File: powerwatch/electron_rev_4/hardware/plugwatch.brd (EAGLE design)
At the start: 52.8 x 90.9 mm, 125 parts, among them J1 DM3AT-SF-PEJM5, Q1 SI223DDS, U1 BGA725L6-ALT, U10 SIP32510, U11 SN74AHC1G04DCKR, U12 SIP32510, U13 AB1815-T3, U16 MAX6746, U2 SAFFB1G56KB0F0A, U3 IRM-03-5V, U4 MAX-M8, U5 MAX9910, U6 LIS2DW12, U8 MAX9910, U9 SIP32510, X1 ABS07-32.768KHZ-7-T

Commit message: doing routing
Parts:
- removed Q1: SI223DDS, fets:SOT23-3
- removed R20: 10k, passives:0402_RES
- removed SJ1: (no value), jumper:SJW
- removed U11: SN74AHC1G04DCKR, chips:SC70
- added C4: 1uF, passives:0402_CAP
- C1, C24, C29, C3: device passives:0603_CAP -> passives:0402_CAP
- moved R1 90.3 mm to (30.0, 61.2), turned to 90 degrees
- moved C19 62.5 mm to (21.6, 72.6), flipped to the top, turned to 0 degrees
- moved C13 58.4 mm to (21.6, 69.2), flipped to the top, turned to 0 degrees
- moved TP13 57.7 mm to (-15.2, 17.0)
- moved R10 51.4 mm to (19.6, 67.6), flipped to the top, turned to 180 degrees
- moved R9 50.7 mm to (23.0, 67.6), flipped to the top, turned to 0 degrees
- moved ASSY1 50.4 mm to (51.7, 84.6), turned to 180 degrees
- moved C100 47.9 mm to (41.8, 9.40), turned to 270 degrees
- moved RI4 44.4 mm to (39.2, 9.40), turned to 270 degrees
- moved R18 42.0 mm to (39.9, 53.5), flipped to the top
- moved RI3 41.0 mm to (36.7, 9.40), turned to 270 degrees
- moved R6 40.9 mm to (3.94, 74.9), turned to 180 degrees
- moved C7 38.6 mm to (50.4, 15.7)
- moved R19 37.7 mm to (51.9, 61.6), flipped to the top, turned to 270 degrees
- moved RF1 37.5 mm to (34.2, 9.40), turned to 270 degrees
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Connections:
- removed net !RTC_INT2: R20.2, U13.4
- removed net N$35: J4.2, Q1.3, SJ1.2
- removed net N$9: Q1.1, U11.4
- net !EXTERNAL_RST: no longer U11.2
- net GND: now also C4.2; no longer U11.3
- net N$23: now also J4.2; no longer Q1.2, SJ1.1, U11.5
- net VCC: now also C4.1; no longer R20.1
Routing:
- net WDI: track 0.00 -> 63.3 mm
- net WIFI_PWR_EN: track 12.9 -> 72.9 mm
- net WIFI_TXD: track 10.8 -> 56.0 mm
- net !RTC_INT1: track 0.00 -> 44.2 mm, vias 0 -> 1
- net WIFI_RXD: track 1.80 -> 45.2 mm
- net SD_MOSI: track 5.78 -> 44.1 mm, vias 2 -> 1
- net SD_MISO: track 6.63 -> 44.0 mm
- net N$23: track 0.00 -> 34.8 mm
- net VCC: track 10.8 -> 41.1 mm, vias 2 -> 5
- net SD_SCLK: track 0.69 -> 25.5 mm, vias 2 -> 0
- net !EXTERNAL_RST: track 0.00 -> 21.7 mm, vias 0 -> 1
- net !GPS_RESET: track 7.07 -> 28.5 mm
- net MIC_WS: track 0.00 -> 20.6 mm
- net GPS_PWR_EN: track 6.30 -> 23.6 mm
- net GPS_VCC: track 19.8 -> 3.14 mm
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- added copper zone on layer 1, net GPS_VCC

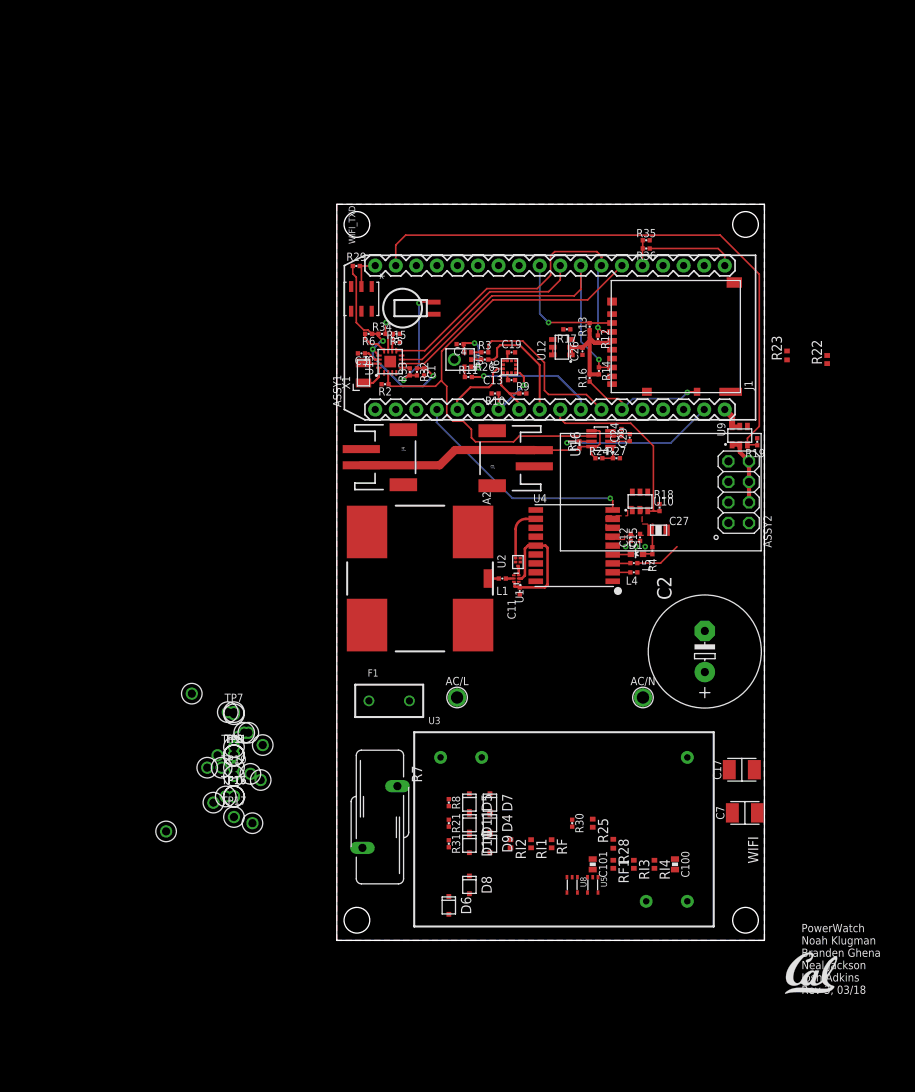
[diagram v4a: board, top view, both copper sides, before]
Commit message: almost finished routing - still need to do debug signals
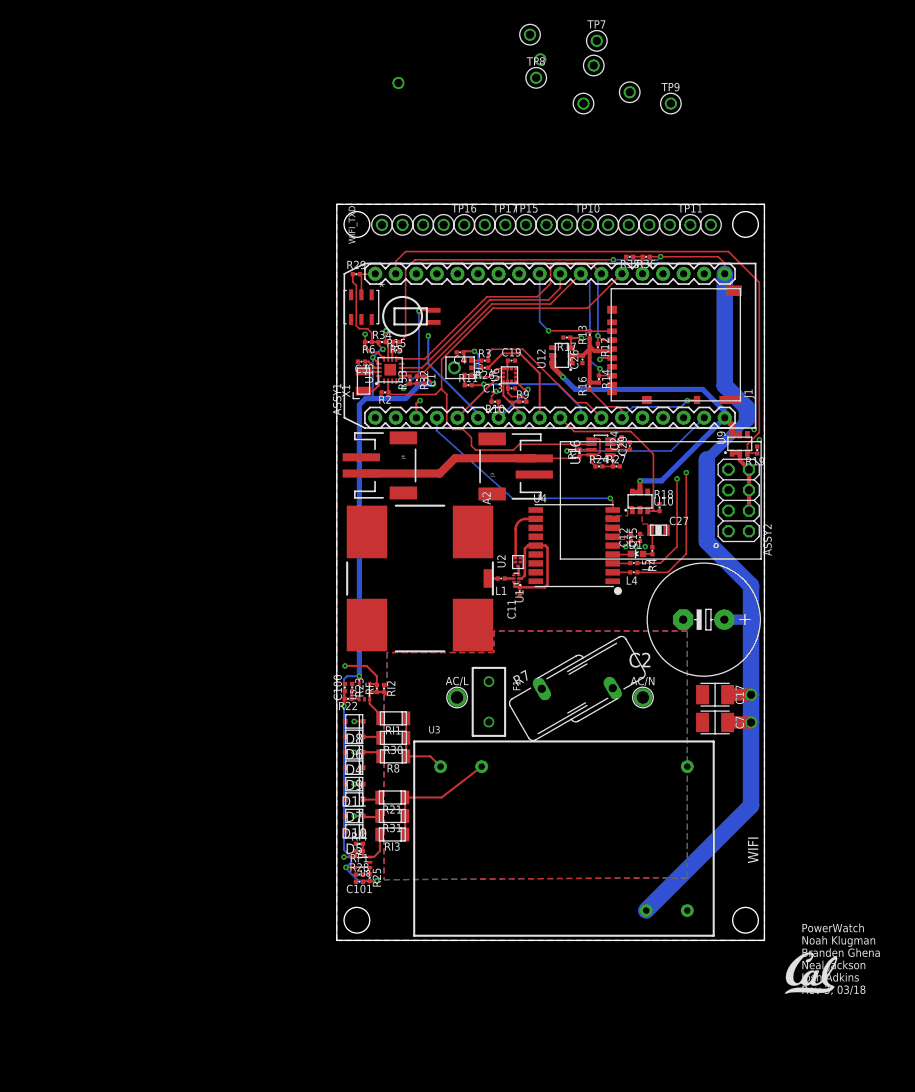
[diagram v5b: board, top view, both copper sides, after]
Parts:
- C100, C101: device passives:0603_CAP -> passives:0402_CAP
- J1: value DM3AT-SF-PEJM5 -> CON_MICRO_SDDM3AT-SF-PEJM5
- R21, R30, R31, R8: device passives:0402_RES -> passives:1206_RES_HIGH_CLEARANCE
- R22, R25, RF, RF1, RI2, RI4: device rcl:R0402 -> passives:0402_RES
- R23, R28: device rcl:R0402_SM -> passives:0402_RES
- RI1, RI3: device rcl:R0402 -> passives:1206_RES_HIGH_CLEARANCE
- U5, U8: value MAX9910 -> OPA369
- moved TP9 96.9 mm to (41.3, 103.4)
- moved TP7 94.5 mm to (32.1, 111.1)
- moved TP18 92.3 mm to (36.2, 104.8)
- moved TP1 91.6 mm to (23.9, 111.9)
- moved TP5 91.6 mm to (25.1, 108.8)
- moved TP8 91.6 mm to (24.6, 106.6)
- moved TP26 91.4 mm to (31.8, 108.1)
- moved TP24 88.1 mm to (41.1, 88.4)
- moved TP4 88.1 mm to (30.5, 103.4)
- moved TP2 87.4 mm to (46.2, 88.4)
- moved TP11 86.5 mm to (43.7, 88.4)
- moved TP3 86.0 mm to (7.62, 105.9)
- moved TP23 85.4 mm to (38.6, 88.4)
- moved TP6 82.9 mm to (36.1, 88.4)
- moved TP10 80.9 mm to (31.0, 88.4)
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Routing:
- net VCC: track 41.1 -> 195.4 mm, vias 5 -> 12
- net 5V: track 10.9 -> 151.1 mm, vias 0 -> 4
- net AC/N-PERTURB: track 0.00 -> 87.4 mm, vias 0 -> 1
- net AC/N-SENSE: track 0.00 -> 83.3 mm, vias 0 -> 1
- net AC/N-MEASURE: track 0.00 -> 82.5 mm, vias 0 -> 1
- net AC/L-PERTURB: track 0.00 -> 81.7 mm, vias 0 -> 1
- net AC/L-MEASURE: track 0.00 -> 75.0 mm, vias 0 -> 1
- net AC/L-SENSE: track 0.00 -> 70.7 mm, vias 0 -> 1
- net GPS_TXD: track 0.00 -> 42.8 mm, vias 0 -> 1
- net AC/N-FUSED: track 0.00 -> 39.7 mm
- net GPS_RXD: track 5.74 -> 41.9 mm, vias 0 -> 1
- net SD_ENABLE: track 0.00 -> 28.8 mm, vias 0 -> 2
- net AC/L-FUSED: track 0.00 -> 26.0 mm
- net !RTC_CS: track 3.55 -> 26.4 mm, vias 0 -> 2
- net SD_SCLK: track 25.5 -> 39.7 mm, vias 0 -> 1
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- added copper zone on layer 1, net N$7
- added copper zone on layer 15, net N$7
- added copper zone on layer 16, net N$7
- added copper zone on layer 2, net N$7

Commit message: layed out debug header, most of the way done routing
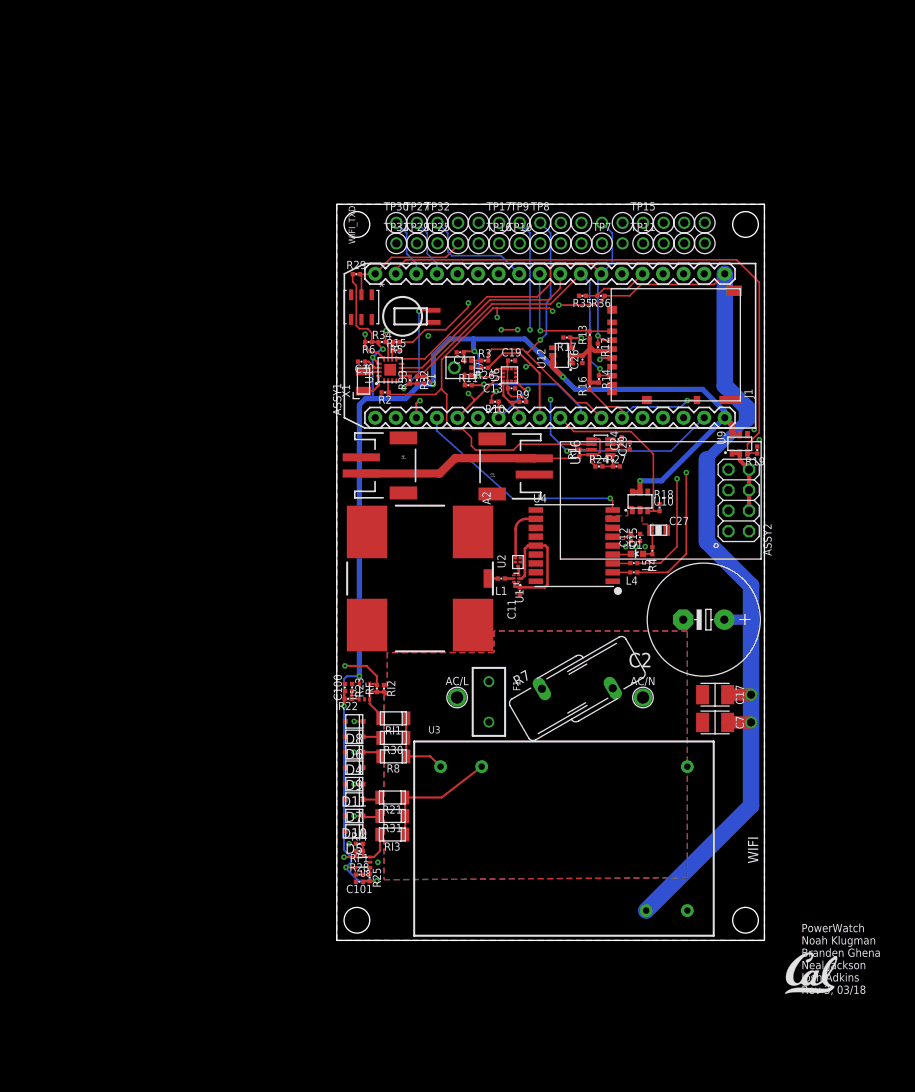
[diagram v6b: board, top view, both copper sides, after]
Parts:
- added TP25, TP27, TP29, TP30, TP31, TP32: TEST_POINT_0.040IN, headers:TESTPOINT_0.040IN
- moved TP3 30.5 mm to (32.8, 88.6)
- moved TP1 30.1 mm to (42.9, 88.6)
- moved TP26 25.9 mm to (45.5, 86.1)
- moved TP7 25.0 mm to (32.8, 86.1)
- moved TP5 24.9 mm to (35.3, 86.1)
- moved TP9 23.8 mm to (22.6, 88.6)
- moved TP18 18.6 mm to (45.5, 88.6)
- moved TP8 17.9 mm to (25.1, 88.6)
- moved TP4 15.5 mm to (35.3, 88.6)
- moved TP15 14.5 mm to (37.8, 88.6)
- moved TP24 10.9 mm to (30.2, 88.6)
- moved TP14 9.67 mm to (17.5, 86.1)
- moved TP19 9.67 mm to (27.7, 86.1)
- moved TP28 9.67 mm to (15.0, 86.1)
- moved TP10 8.69 mm to (22.6, 86.1)
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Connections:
- net AC/L-MEASURE: now also TP29.TESTPOINT
- net AC/L-PERTURB: now also TP25.TESTPOINT
- net AC/L-SENSE: now also TP31.TESTPOINT
- net AC/N-MEASURE: now also TP27.TESTPOINT
- net AC/N-PERTURB: now also TP32.TESTPOINT
- net AC/N-SENSE: now also TP30.TESTPOINT
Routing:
- net !EXTERNAL_RST: track 21.7 -> 53.4 mm, vias 1 -> 2
- net ACCEL_INT: track 7.76 -> 38.9 mm, vias 0 -> 1
- net WIFI_TXD: track 56.0 -> 85.8 mm
- net WIFI_RXD: track 45.2 -> 70.9 mm
- net VCC: track 195.4 -> 220.9 mm
- net MIC_BCLK: track 16.0 -> 38.4 mm, vias 1 -> 3
- net MIC_DATA: track 13.6 -> 33.0 mm, vias 0 -> 2
- net MIC_WS: track 18.6 -> 36.6 mm, vias 0 -> 1
- net AC/N-PERTURB: track 87.4 -> 101.4 mm
- net SERIAL_NUM: track 4.55 -> 16.5 mm
- net WDI: track 63.3 -> 75.0 mm, vias 0 -> 2
- net WIFI_PWR_EN: track 71.4 -> 82.2 mm
- net SD_MISO: track 42.4 -> 51.8 mm
- net AC/L-MEASURE: track 75.0 -> 84.4 mm
- net SD_SCLK: track 39.7 -> 48.9 mm
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
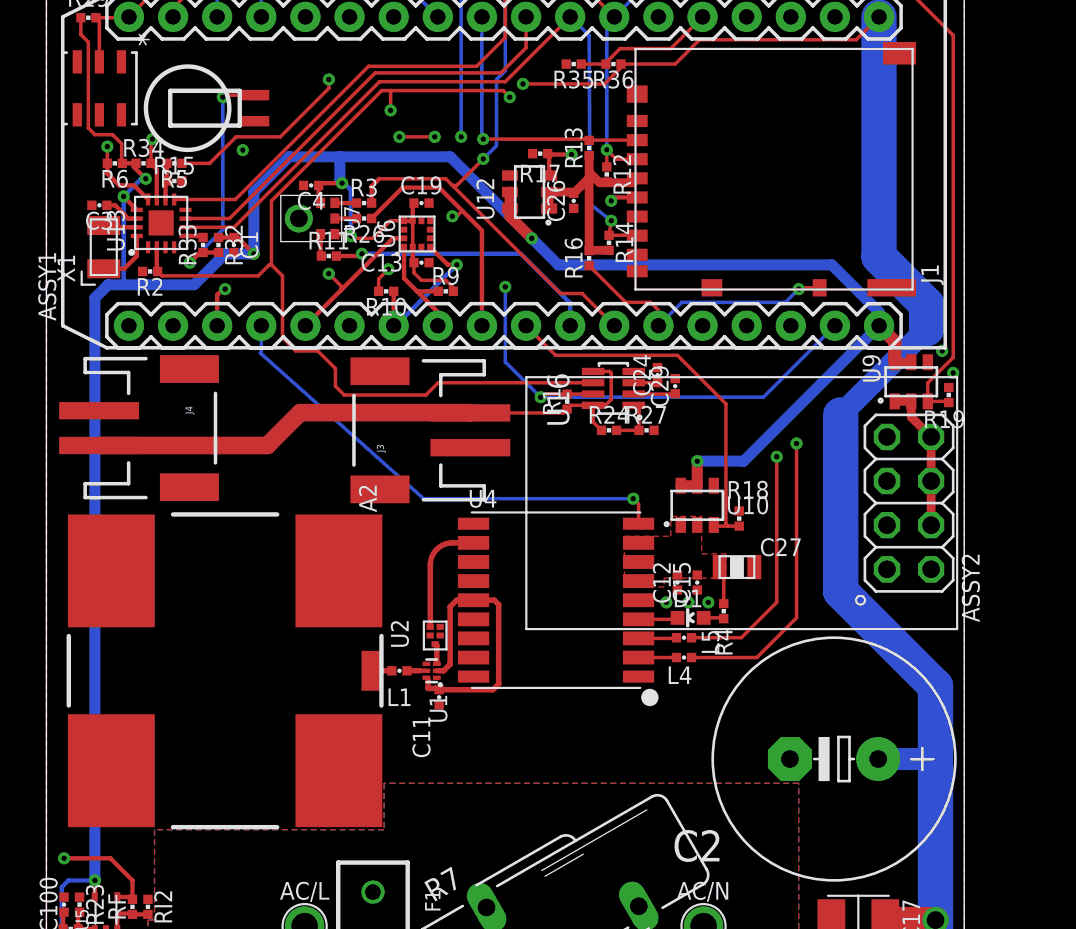
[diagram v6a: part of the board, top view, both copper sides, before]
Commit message: only 4 more airwires
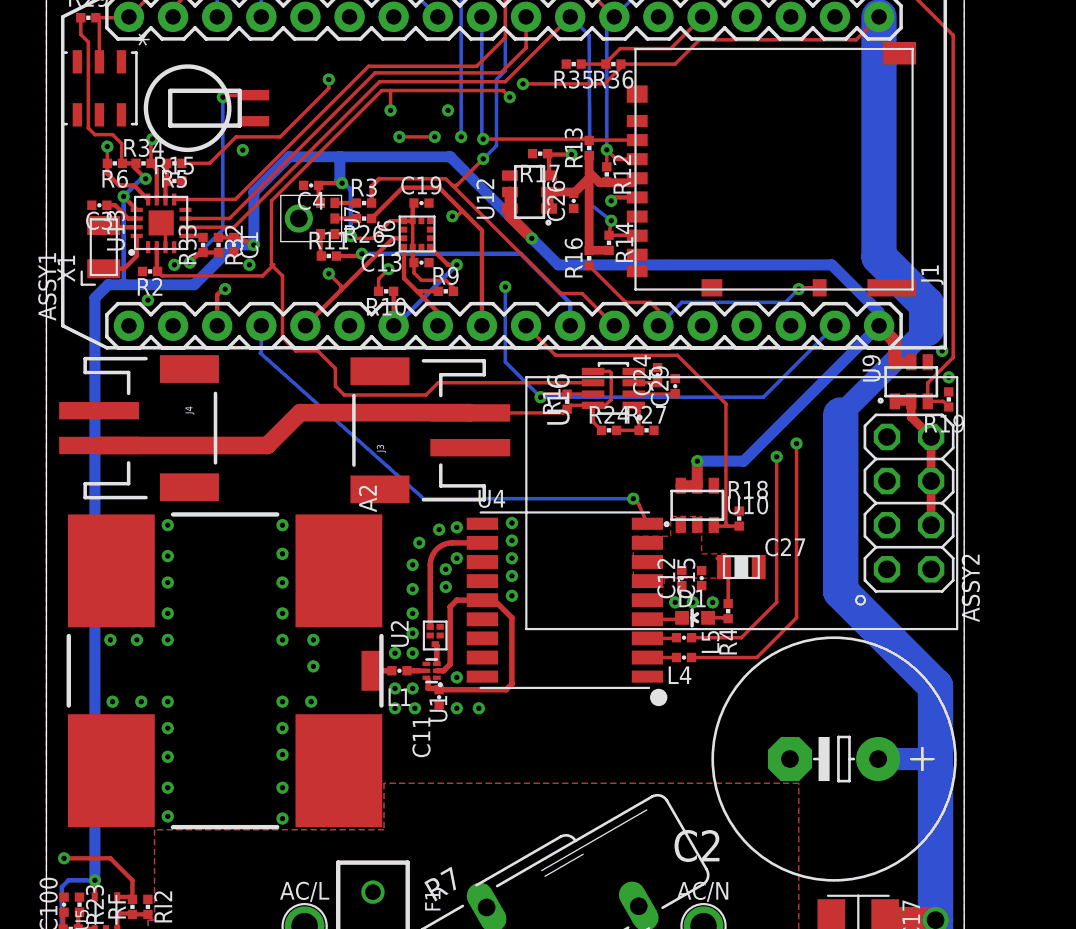
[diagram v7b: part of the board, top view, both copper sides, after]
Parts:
- moved U4 0.51 mm to (29.8, 48.8)
- moved C12 0.36 mm to (36.6, 50.0)
- moved C15 0.36 mm to (37.7, 50.0)
- moved C27 0.25 mm to (40.0, 50.7)
- moved R4 0.25 mm to (39.2, 48.1)
- moved D1 0.25 mm to (37.3, 47.8)
- moved R19 0.25 mm to (51.9, 60.3)
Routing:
- net GPS_PWR_EN: track 21.9 -> 60.0 mm
- net !RTC_CS: track 26.4 -> 61.5 mm, vias 2 -> 3
- net !GPS_RESET: track 27.8 -> 62.2 mm
- net !RTC_INT1: track 44.2 -> 67.6 mm
- net MIC_BCLK: track 38.4 -> 40.7 mm
- net GND: track 0.00 -> 1.50 mm, vias 7 -> 61
- net VCC_RF: track 16.7 -> 17.8 mm
- net WIFI_RXD: track 70.9 -> 71.8 mm
- net VCC: track 220.9 -> 220.3 mm
- net GPS_RF_IN: track 6.58 -> 7.09 mm
- net N$41: track 2.20 -> 1.69 mm
- net N$40: track 2.18 -> 1.68 mm

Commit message: fixed based on case, rerouted, some of the silk
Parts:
- removed SERIAL: DS2401P+, DS2401P+:21-0382
- added U20: DS2401P+, DS2401P+:21-0382
- moved TP31 10.1 mm to (14.0, 93.7)
- moved TP26 7.69 mm to (44.5, 93.7)
- moved TP30 6.51 mm to (11.4, 93.7)
- moved TP18 6.20 mm to (41.9, 93.7)
- moved TP1 2.96 mm to (44.5, 91.2)
- moved TP11 2.96 mm to (39.4, 88.6)
- moved TP12 2.96 mm to (16.5, 91.2)
- moved TP13 2.96 mm to (19.1, 91.2)
- moved TP14 2.96 mm to (19.1, 88.6)
- moved TP15 2.96 mm to (39.4, 91.2)
- moved TP16 2.96 mm to (21.6, 88.6)
- moved TP17 2.96 mm to (21.6, 91.2)
- moved TP19 2.96 mm to (29.2, 88.6)
- moved TP2 2.96 mm to (44.5, 88.6)
- moved TP20 2.96 mm to (29.2, 91.2)
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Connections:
- net GND: now also U20.1; no longer SERIAL.1
- net SERIAL_NUM: now also U20.2; no longer SERIAL.2
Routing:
- net SENSORS_SCL: track 6.56 -> 42.0 mm, vias 0 -> 1
- net SENSORS_SDA: track 9.03 -> 35.2 mm, vias 1 -> 2
- net !SD_DETECT: track 16.1 -> 39.8 mm, vias 1 -> 2
- net SD_ENABLE: track 28.8 -> 43.3 mm
- net AC/L-SENSE: track 72.6 -> 81.2 mm
- net VCC: track 220.3 -> 225.3 mm
- net WIFI_PWR_EN: track 82.3 -> 87.3 mm
- net !EXTERNAL_RST: track 53.4 -> 56.9 mm
- net SD_MISO: track 51.8 -> 54.4 mm
- net AC/N-SENSE: track 90.6 -> 93.1 mm
- net AC/N-FUSED: track 39.7 -> 41.7 mm
- net WDI: track 75.2 -> 77.2 mm
- net !SD_CS: track 23.2 -> 25.2 mm
- net SERIAL_NUM: track 16.5 -> 18.4 mm
- net WIFI_TXD: track 85.8 -> 87.6 mm
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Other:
- board size 52.8 x 90.9 mm -> 55.7 x 95.2 mm
- board text removed: "WIFI"
- board text removed: "WIFI_TXD"
